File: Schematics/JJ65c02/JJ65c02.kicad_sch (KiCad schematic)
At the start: 24 parts, among them U1 74HC08

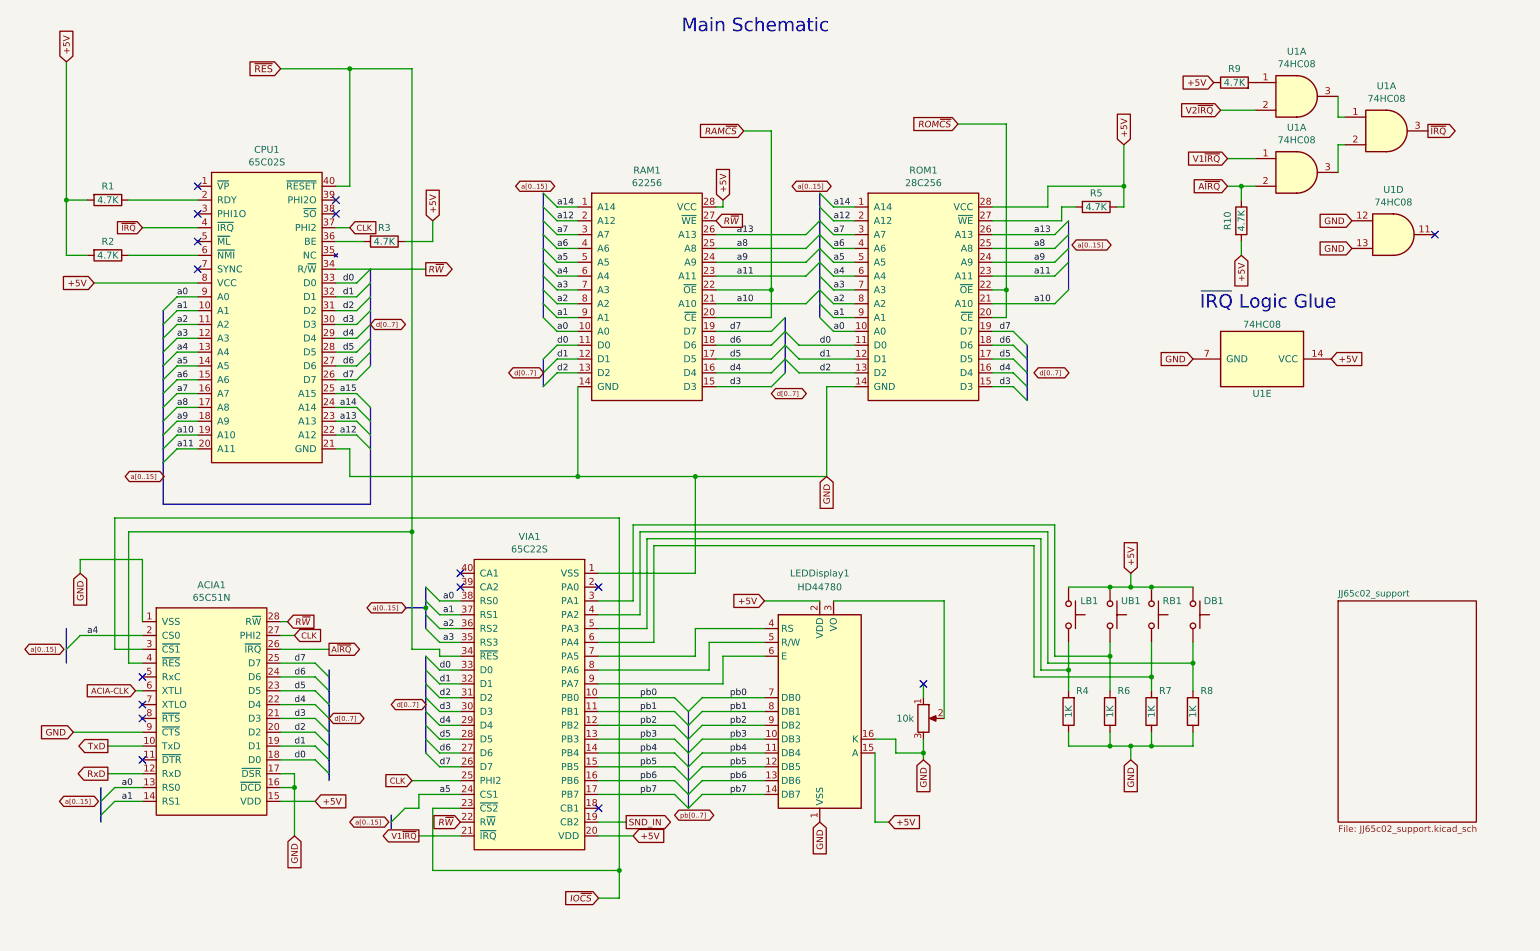
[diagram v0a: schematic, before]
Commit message: We are no longer bit-bashing sound on the VIA chip. Keep the files for future generations
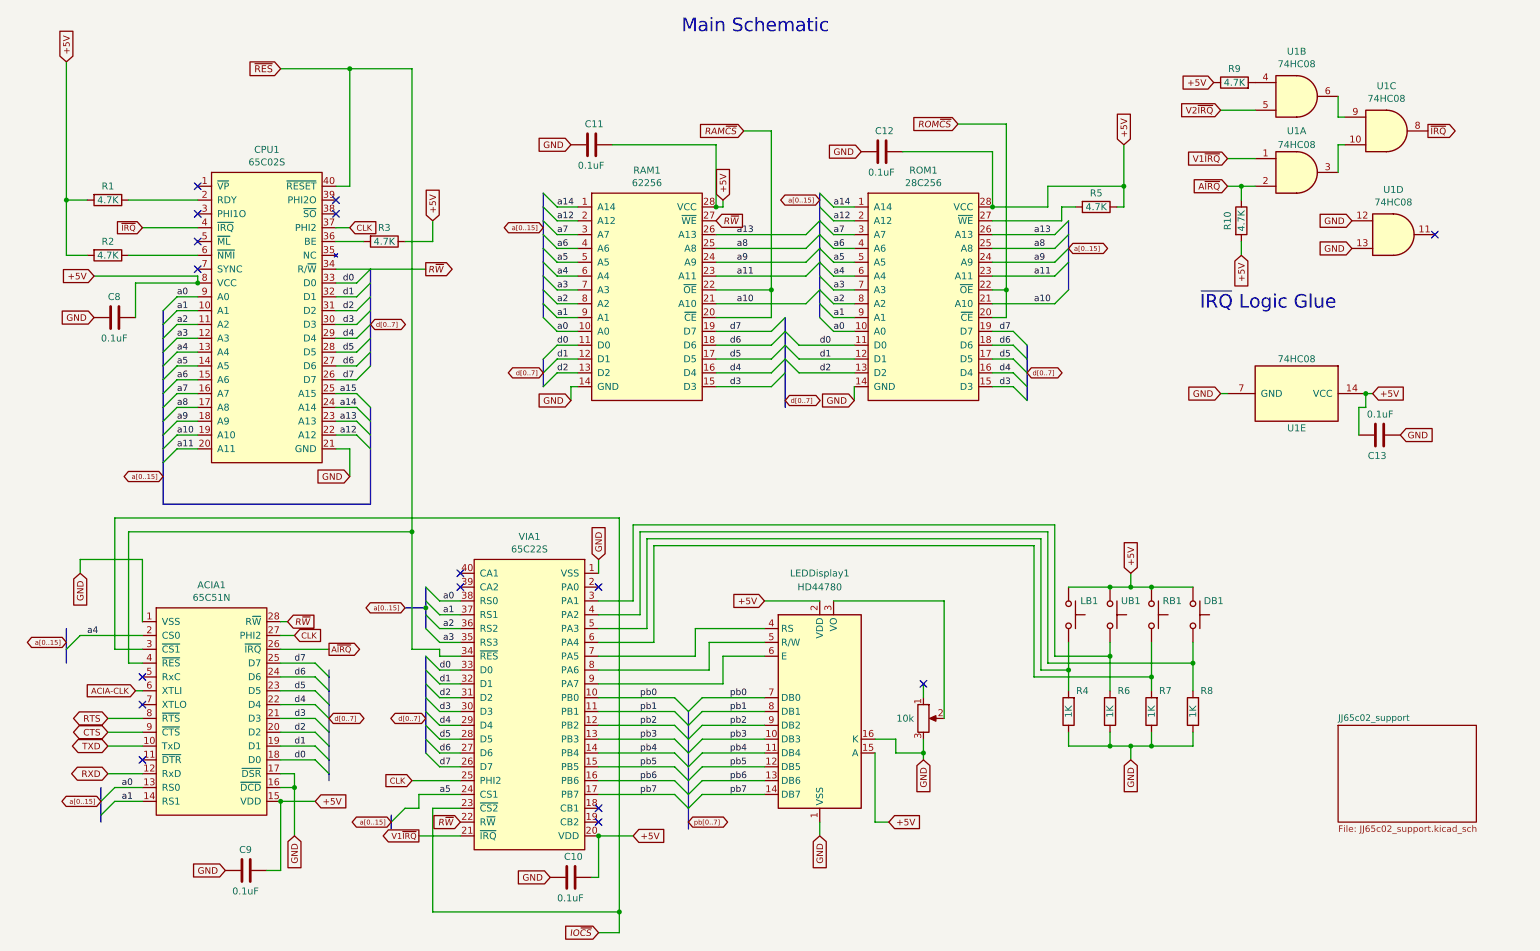
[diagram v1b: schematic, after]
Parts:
- added C10, C11, C12, C13, C8, C9: 0.1uF, Capacitor_THT:C_Disc_D4.7mm_W2.5mm_P5.00mm, symbol Device:C
- LEDDisplay1: symbol Display_Character:NHD-0420H1Z -> JJ65c02-rescue:NHD-0420H1Z
- ROM1: footprint Socket:DIP_Socket-28_W11.9_W12.7_W15.24_W17.78_W18.5_3M_228-1277-00-0602J -> Package_DIP:DIP-28_W15.24mm_Socket
- RV1: symbol Device:R_POT -> Device:R_Potentiometer
- U1: symbol 74xx:74LS08 -> JJ65c02-rescue:74HC08
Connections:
- net +5V: now also C10.1, C11.1, C12.1, C13.1, C8.1, C9.1
- net GND: now also C10.2, C11.2, C12.2, C13.2, C8.2, C9.2; no longer ACIA1.9 (~{CTS})
- net V2~{IRQ}: now also U1.5; no longer U1.2
- net ~{IRQ}: now also U1.8; no longer U1.3
- net RTS: now reaches ACIA1.8 (~{RTS})
- net at U1.3: now also U1.10; no longer U1.2
- net at R9.2: now also U1.4; no longer U1.1
- net RxD renamed RXD
- net SND_IN: no longer names the net of VIA1.19 (CB2)
- net TxD renamed TXD
- new net: U1.6, U1.9
- new net CTS: ACIA1.9 (~{CTS})
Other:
- moved on the sheet: U1E

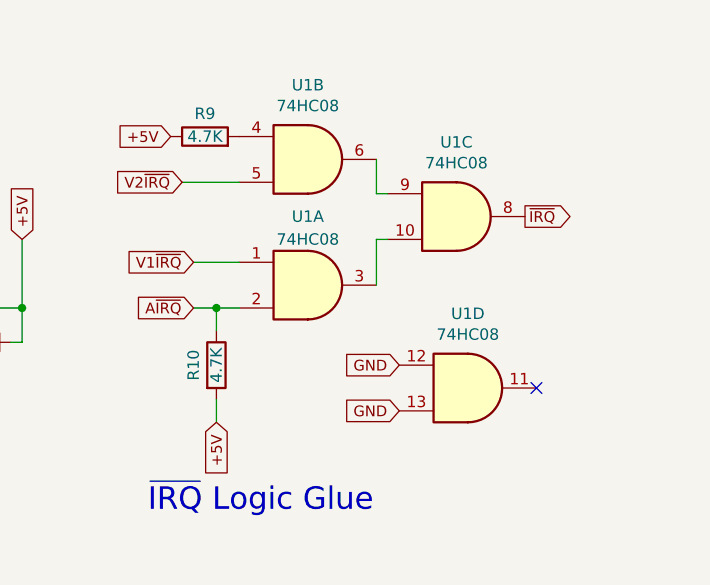
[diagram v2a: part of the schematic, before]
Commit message: Prep for latest round of work:   o Use WinCUPL and ATF22V10C for address decoding   o More RAM and less ROM - new memory map!   o No onboard speaker... wastes space on board
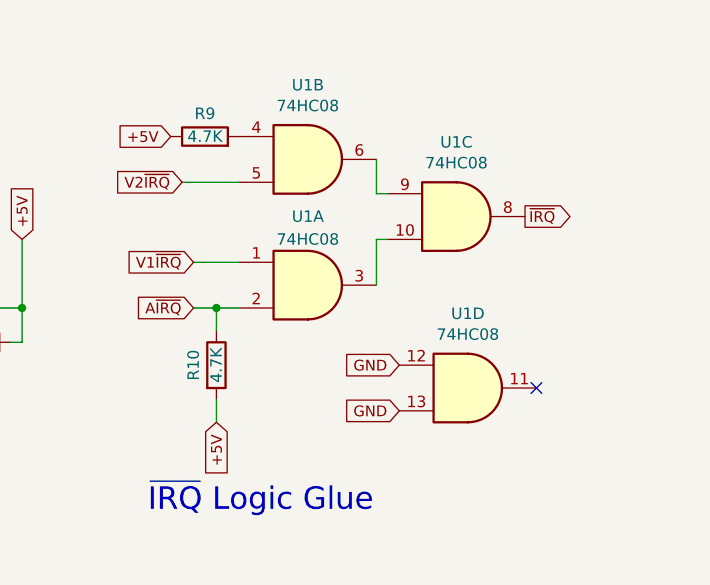
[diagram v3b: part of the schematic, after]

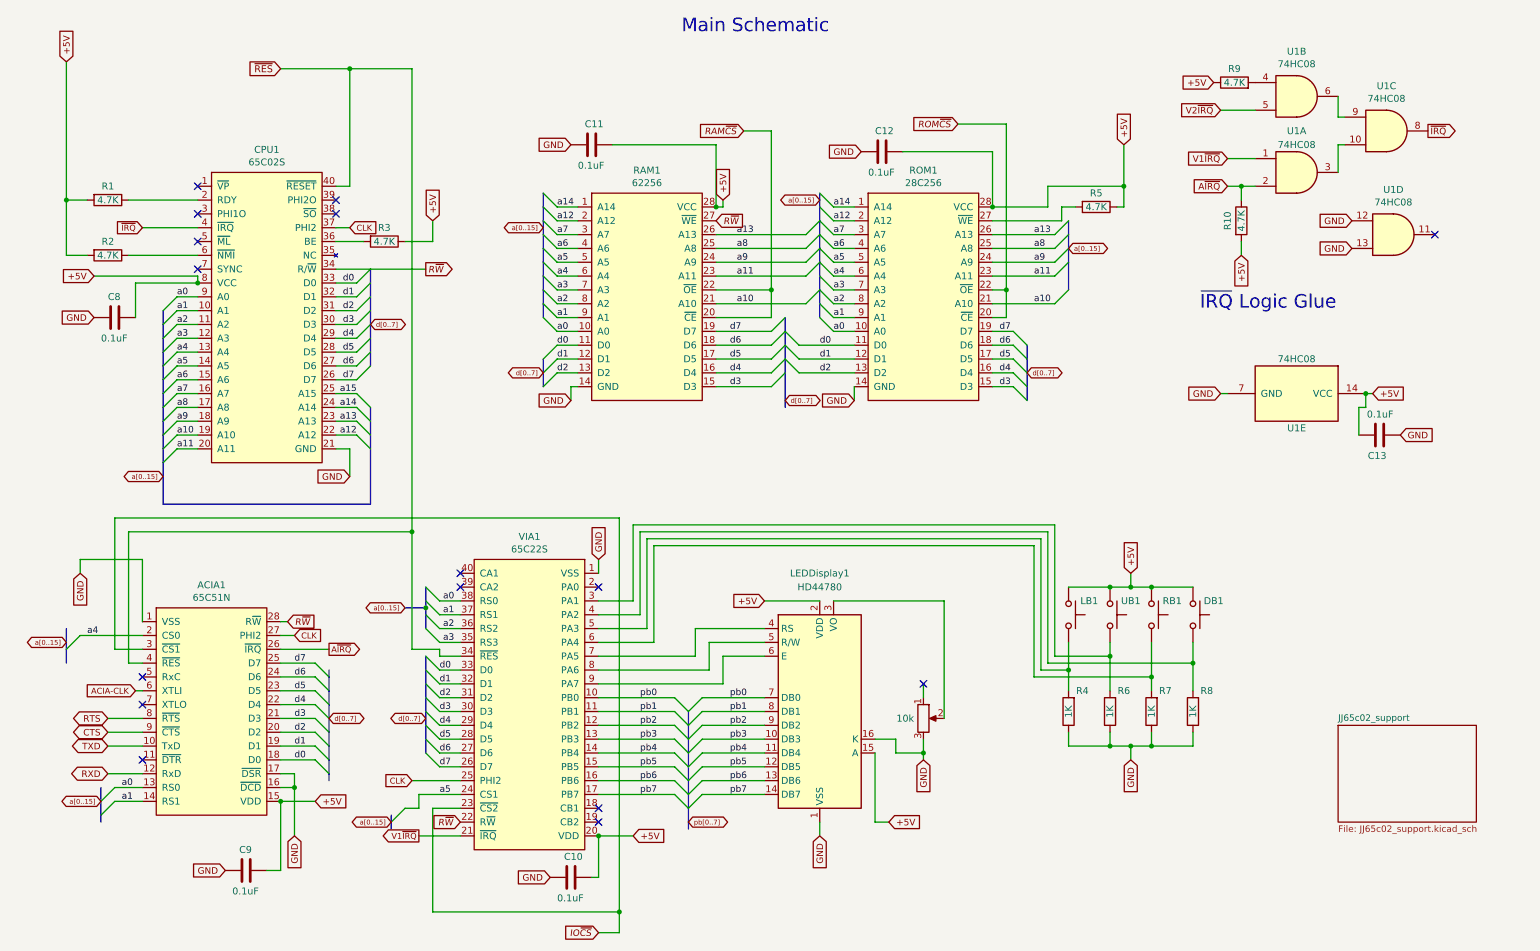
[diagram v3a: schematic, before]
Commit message: Refresh with current Schematics and wire-paths
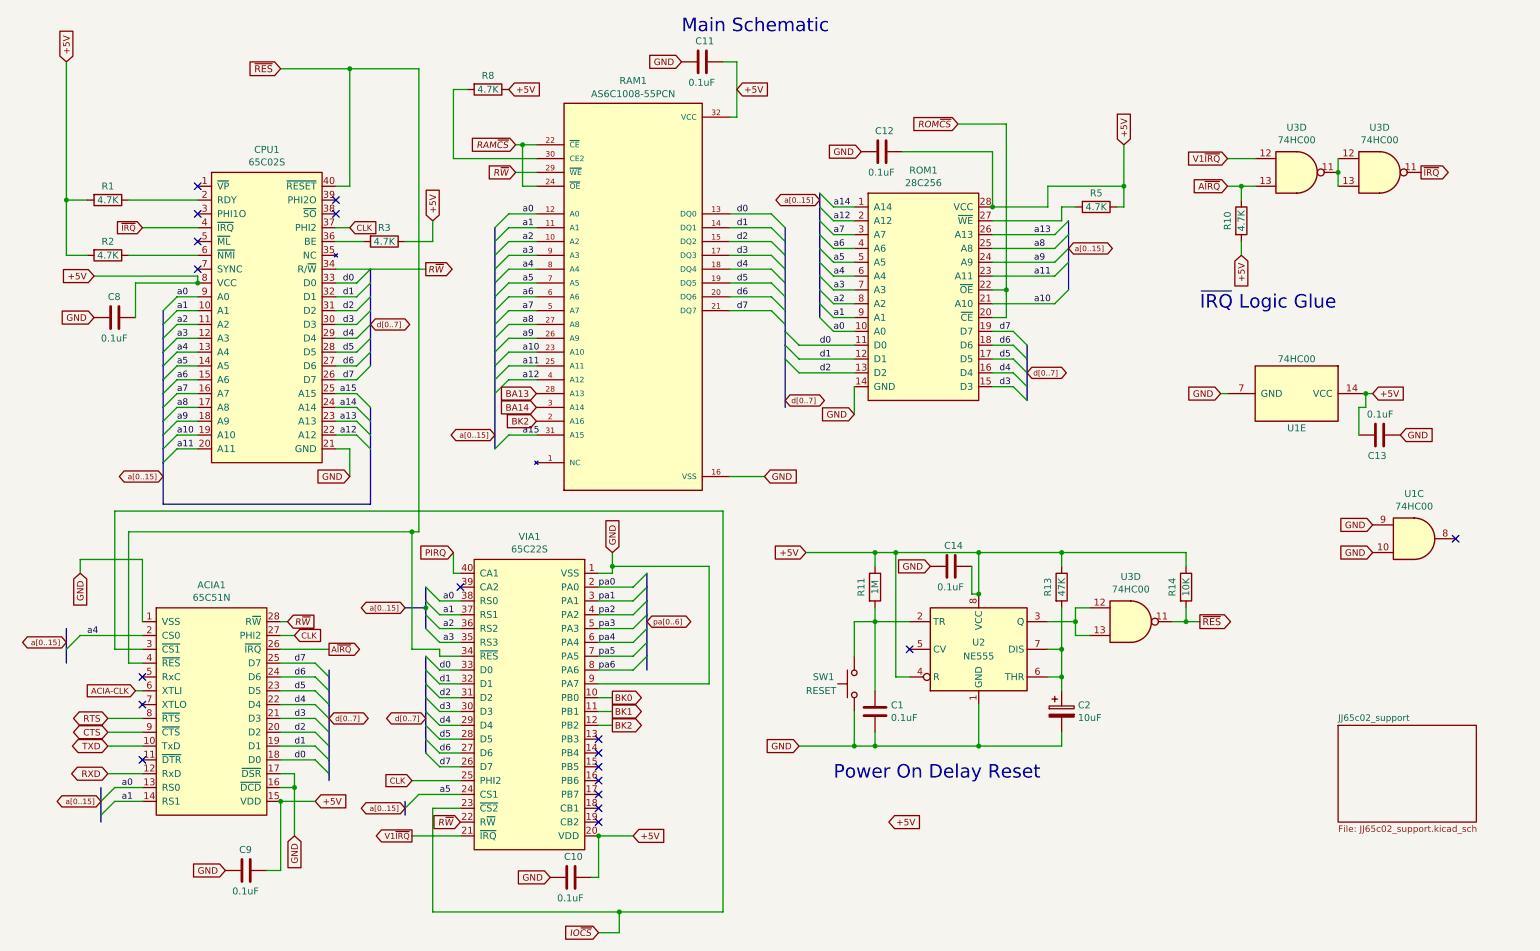
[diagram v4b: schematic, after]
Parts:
- removed DB1, LB1, RB1, UB1: SW_Push, Button_Switch_THT:SW_PUSH_6mm, symbol Switch:SW_Push
- removed LEDDisplay1: HD44780, JJ65c02:LCD-20x4v2, symbol JJ65c02-rescue:NHD-0420H1Z
- removed R4, R6, R7: 1K, Resistor_THT:R_Axial_DIN0207_L6.3mm_D2.5mm_P7.62mm_Horizontal, symbol Device:R
- removed R9: 4.7K, Resistor_THT:R_Axial_DIN0207_L6.3mm_D2.5mm_P7.62mm_Horizontal, symbol Device:R
- removed RAM1: 62256, Package_DIP:DIP-28_W15.24mm_Socket, symbol 6502:62256
- removed RV1: 10k, Potentiometer_THT:Potentiometer_Bourns_3339P_Vertical, symbol Device:R_Potentiometer
- removed unit 1 of U1
- removed unit 2 of U1
- removed unit 4 of U1
- added C1, C14: 0.1uF, Capacitor_THT:C_Disc_D4.7mm_W2.5mm_P5.00mm, symbol Device:C
- added C2: 10uF, Capacitor_THT:CP_Radial_D5.0mm_P2.50mm, symbol Device:C_Polarized
- added R11: 1M, Resistor_THT:R_Axial_DIN0207_L6.3mm_D2.5mm_P7.62mm_Horizontal, symbol Device:R
- added R13: 47K, Resistor_THT:R_Axial_DIN0207_L6.3mm_D2.5mm_P7.62mm_Horizontal, symbol Device:R
- added R14: 10K, Resistor_THT:R_Axial_DIN0207_L6.3mm_D2.5mm_P7.62mm_Horizontal, symbol Device:R
- added RAM1: AS6C1008-55PCN, DIP1524W45P254L4191H419Q32, symbol JJ65c02-rescue:AS6C1008-55PCN
- added SW1: RESET, Button_Switch_THT:SW_PUSH_6mm, symbol Switch:SW_Push
- added U2: NE555, Package_DIP:DIP-8_W7.62mm, symbol Timer:LM555xN
- added U3 (x3): 74HC00, Package_DIP:DIP-14_W7.62mm_Socket, symbol 74xx:74HC00
- R8: value 1K -> 4.7K
- U1: value 74HC08 -> 74HC00
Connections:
- net +5V: now also R8.1, C14.1, R11.1, R13.1, R14.1, RAM1.32 (VCC), U2.4 (R), U2.8 (VCC)
- net A~{IRQ}: now also U3.13
- net GND: now also U1.10, U1.9, VIA1.9 (PA7), C1.2, C14.2, C2.2, RAM1.16 (VSS), SW1.1, U2.1 (GND); no longer R8.1
- net RAM~{CS}: now also RAM1.22 (~{CE}), RAM1.24 (~{OE})
- net R~{W}: now also RAM1.29 (~{WE})
- net V1~{IRQ}: now also U3.12
- net a0: now also RAM1.12 (A0)
- net a1: now also RAM1.11 (A1)
- net a10: now also RAM1.23 (A10)
- net a11: now also RAM1.25 (A11)
- net a12: now also RAM1.4 (A12)
- net a15: now also RAM1.31 (A15)
- net a2: now also RAM1.10 (A2)
- net a3: now also RAM1.9 (A3)
- net a4: now also RAM1.8 (A4)
- net a5: now also RAM1.7 (A5)
- net a6: now also RAM1.6 (A6)
- net a7: now also RAM1.5 (A7)
- net a8: now also RAM1.27 (A8)
- net a9: now also RAM1.26 (A9)
- net d0: now also RAM1.13 (DQ0)
- net d1: now also RAM1.14 (DQ1)
- net d2: now also RAM1.15 (DQ2)
- net d3: now also RAM1.17 (DQ3)
- net d4: now also RAM1.18 (DQ4)
- net d5: now also RAM1.19 (DQ5)
- net d6: now also RAM1.20 (DQ6)
- net d7: now also RAM1.21 (DQ7)
- net ~{IRQ}: now also U3.11; no longer U1.8
- net ~{RES}: now also R14.2, U3.11
- net pa0: now reaches VIA1.2 (PA0)
- net pa1: now reaches VIA1.3 (PA1)
- net at R8.2: now also RAM1.30 (CE2); no longer VIA1.4 (PA2)
- net PIRQ: now reaches VIA1.40 (CA1)
- net pa3: now reaches VIA1.5 (PA3)
- net pa4: now reaches VIA1.6 (PA4)
- net pa5: now reaches VIA1.7 (PA5)
- net pa6: now reaches VIA1.8 (PA6)
- net pb0 renamed BK0
- net pb1 renamed BK1
- net pb2 renamed BK2
- net BK2: now also RAM1.2 (A16)
- net pb3: no longer names the net of VIA1.13 (PB3)
- net pb4: no longer names the net of VIA1.14 (PB4)
- net pb5: no longer names the net of VIA1.15 (PB5)
- net pb6: no longer names the net of VIA1.16 (PB6)
- net pb7: no longer names the net of VIA1.17 (PB7)
- new net: U2.3 (Q), U3.12, U3.13
- new net: C2.1, R13.2, U2.6 (THR), U2.7 (DIS)
- new net: C1.1, R11.2, SW1.2, U2.2 (TR)
- new net: U3.11, U3.12, U3.13
- new net BA13: RAM1.28 (A13)
- new net BA14: RAM1.3 (A14)
- new net pa2: VIA1.4 (PA2)
- no-connect marks 16 -> 19
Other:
- note added: "Power On Delay Reset"
- moved on the sheet: C11

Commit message: Latest version... ready for PCBs??
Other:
- moved on the sheet: C1, C14, C2, R11, R13, R14, SW1, U2, U3D

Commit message: Update schems - WIP
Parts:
- RAM1: footprint DIP1524W45P254L4191H419Q32 -> JJ65c02:DIP1524W45P254L4191H419Q32
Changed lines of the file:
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@@
       (effects (font (size 1.27 1.27)))
     )
-    (property "Footprint" "DIP1524W45P254L4191H419Q32" (at 125.73 66.04 0)
+    (property "Footprint" "JJ65c02:DIP1524W45P254L4191H419Q32" (at 125.73 66.04 0)
       (effects (font (size 1.27 1.27)) (justify left bottom) hide)
     )
